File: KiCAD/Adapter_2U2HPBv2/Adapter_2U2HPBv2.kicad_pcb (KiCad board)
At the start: 2 copper layers, 9.8 x 84 mm, 2 parts

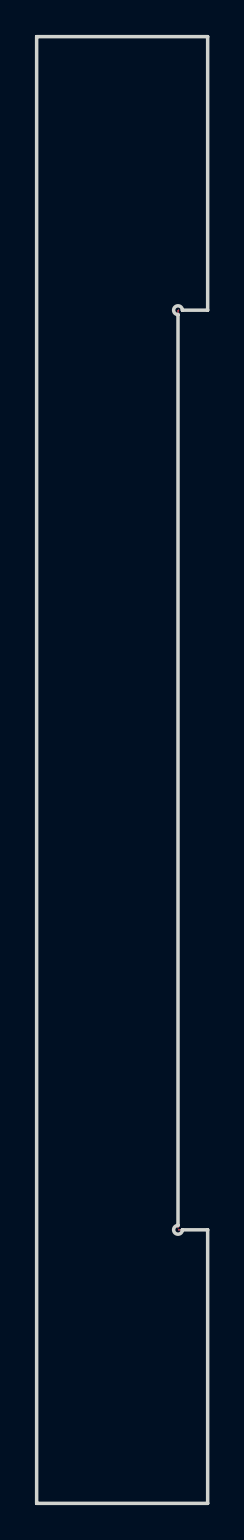
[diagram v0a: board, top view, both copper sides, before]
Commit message: updated all modules to use plated through-holes wherever possible
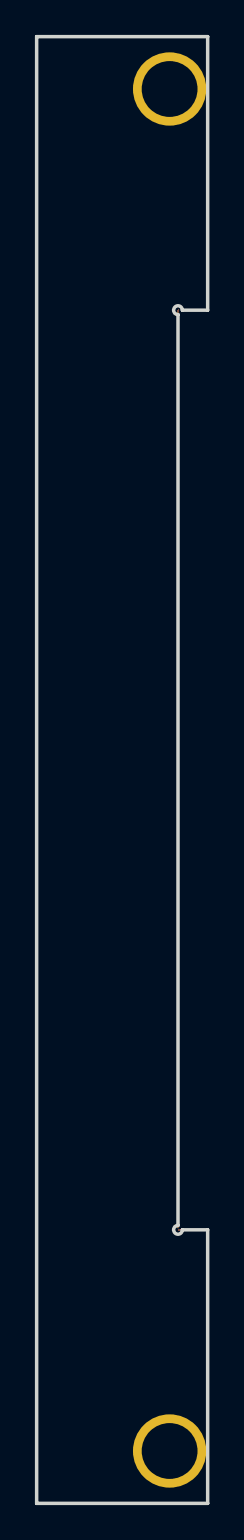
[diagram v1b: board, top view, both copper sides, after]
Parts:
- moved H1 2.54 mm to (7.62, 5.42)
- moved H2 2.54 mm to (7.62, 83.5)
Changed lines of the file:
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@@
 	(footprint "EXC:MountingHole_3.2mm_M3"
 		(layer "F.Cu")
-		(at 5.08 5.425)
+		(at 7.62 5.425)
 		(descr "Mounting Hole 3.2mm, no annular, M3")
 		(tags "mounting hole 3.2mm no annular m3")
@@
 			)
 		)
-		(pad "" np_thru_hole oval
+		(pad "" thru_hole circle
 			(at 0 0)
-			(size 4.34 3.2)
-			(drill oval 4.34 3.2)
+			(size 4.2 4.2)
+			(drill 3.2)
 			(layers "*.Cu" "*.Mask")
+			(remove_unused_layers no)
 		)
 		(embedded_fonts no)
@@
 	(footprint "EXC:MountingHole_3.2mm_M3"
 		(layer "F.Cu")
-		(at 5.08 83.475)
+		(at 7.62 83.475)
 		(descr "Mounting Hole 3.2mm, no annular, M3")
 		(tags "mounting hole 3.2mm no annular m3")
@@
 			)
 		)
-		(pad "" np_thru_hole oval
+		(pad "" thru_hole circle
 			(at 0 0)
-			(size 4.34 3.2)
-			(drill oval 4.34 3.2)
+			(size 4.2 4.2)
+			(drill 3.2)
 			(layers "*.Cu" "*.Mask")
+			(remove_unused_layers no)
 		)
 		(embedded_fonts no)
